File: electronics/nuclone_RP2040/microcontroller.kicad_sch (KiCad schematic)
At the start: 19 parts, among them Y1 12MHz

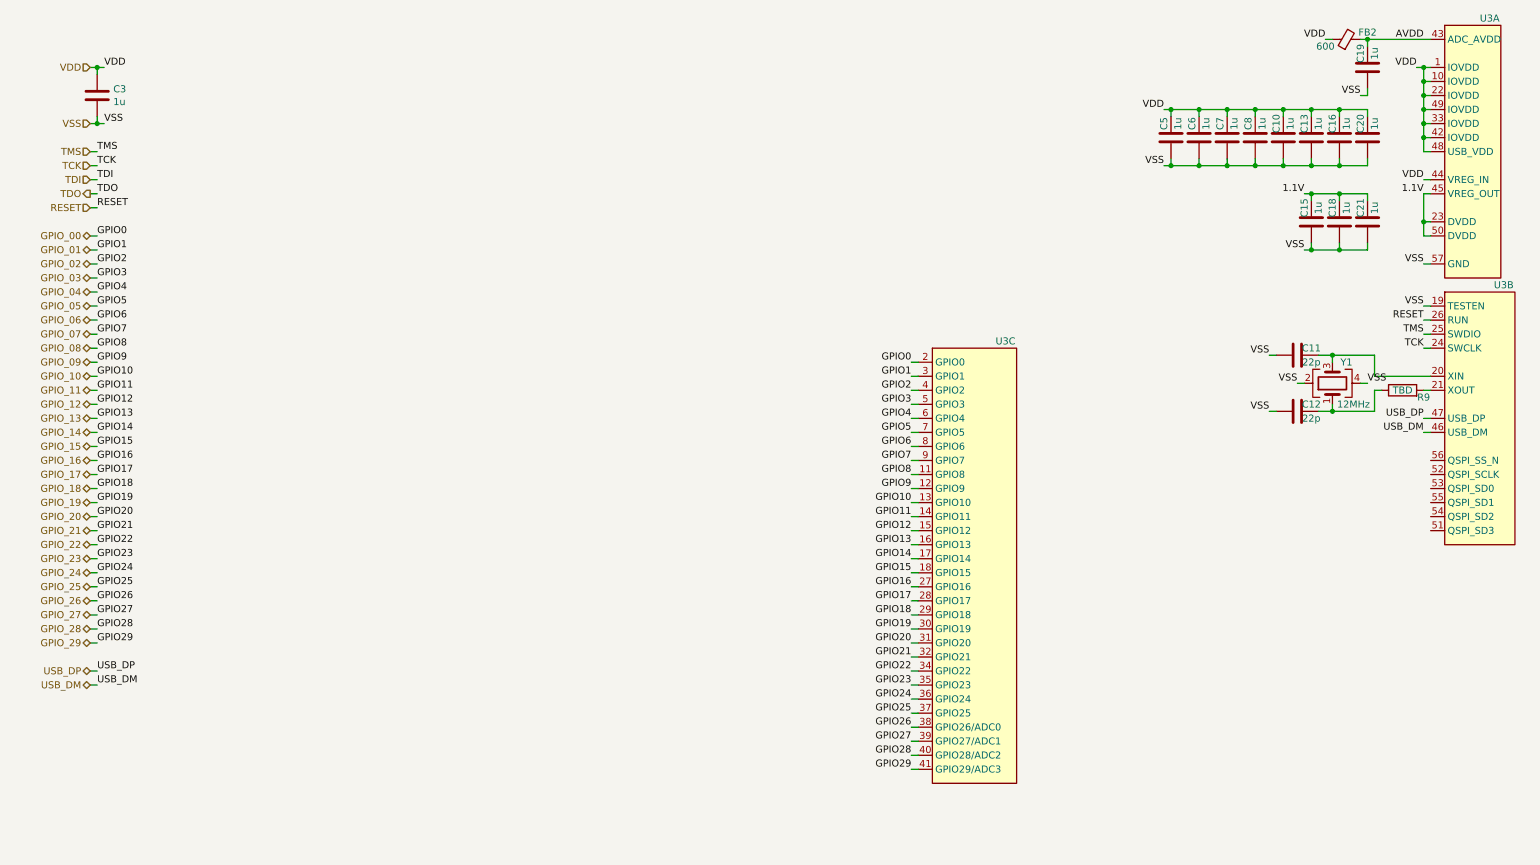
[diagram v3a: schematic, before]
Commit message: added QSPI flash
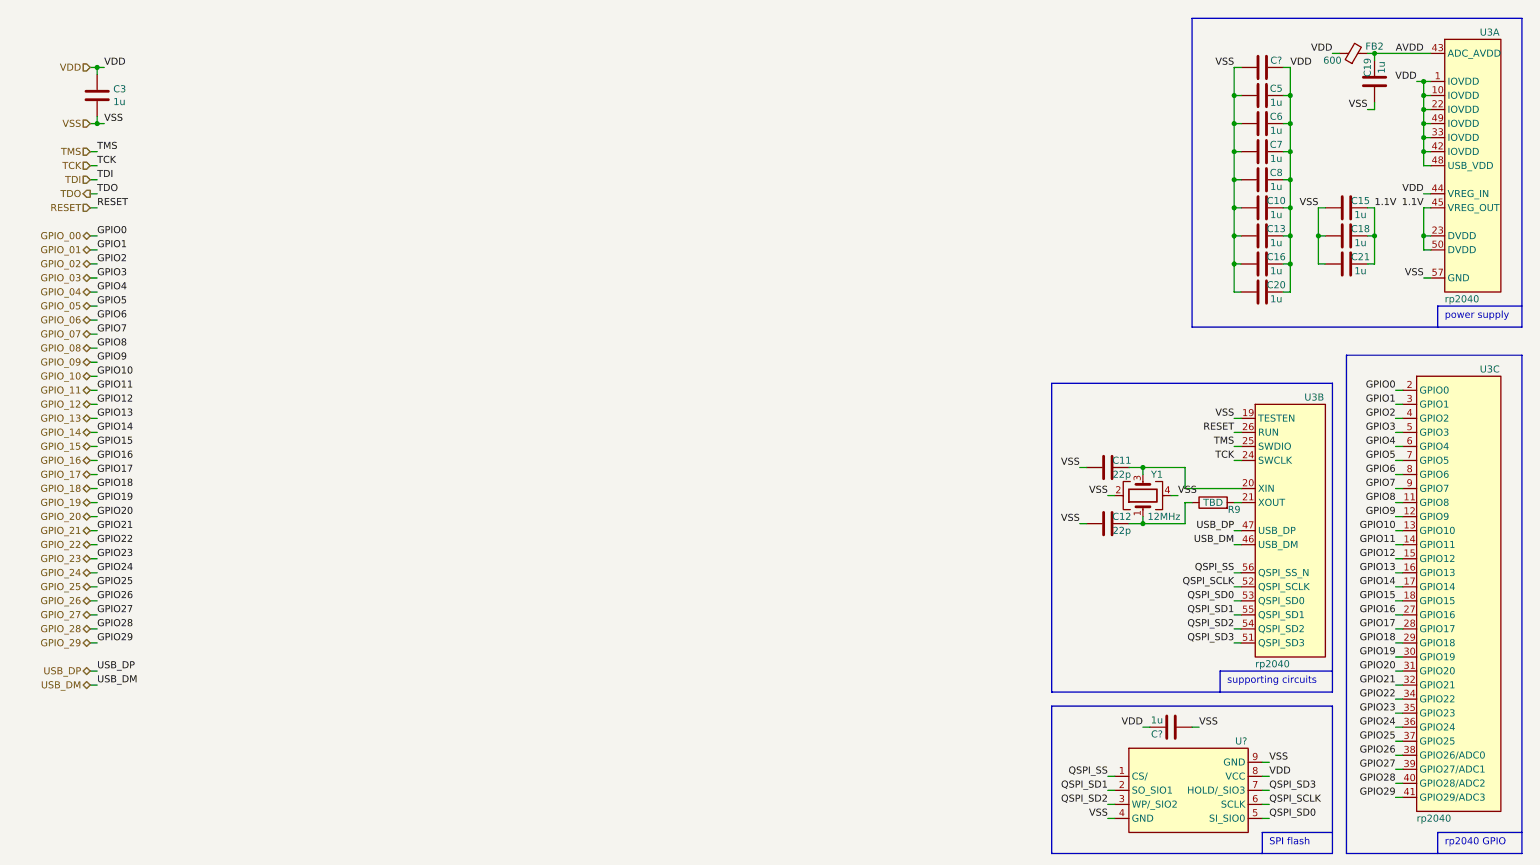
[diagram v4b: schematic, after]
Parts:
- added C?: 1u, SquantorRcl:C_0402, symbol Device:C
- added C?: (no value), symbol Device:C
- added U?: (no value), symbol SquantorGenericDigital:25X_9pin_QSPI_flash
- U3: value (none) -> rp2040; footprint (none) -> SquantorIC:QFN56_7by7mm_RaspberryPi
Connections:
- net VDD: now also C?.2, C?.2, U?.8 (VCC)
- net VSS: now also C?.1, C?.1, U?.4 (GND), U?.9 (GND)
- net QSPI_SD3: now reaches U3.51 (QSPI_SD3)
- net QSPI_SD3: now also U?.7 (HOLD/_SIO3)
- net QSPI_SCLK: now reaches U3.52 (QSPI_SCLK)
- net QSPI_SCLK: now also U?.6 (SCLK)
- net QSPI_SD0: now reaches U3.53 (QSPI_SD0)
- net QSPI_SD0: now also U?.5 (SI_SIO0)
- net QSPI_SD2: now reaches U3.54 (QSPI_SD2)
- net QSPI_SD2: now also U?.3 (WP/_SIO2)
- net QSPI_SD1: now reaches U3.55 (QSPI_SD1)
- net QSPI_SD1: now also U?.2 (SO_SIO1)
- net QSPI_SS: now reaches U3.56 (QSPI_SS_N)
- net QSPI_SS: now also U?.1 (CS/)
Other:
- note added: "SPI flash"
- note added: "power supply"
- note added: "rp2040 GPIO"
- note added: "supporting circuits"
- moved on the sheet: C10, C11, C12, C13, C15, C16, C18, C19, C20, C21, C5, C6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

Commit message: added serial flash
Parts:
- gave numbers to parts that had none: 3
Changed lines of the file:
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@@
   (symbol (lib_id "Device:C") (at 219.71 142.24 270) (unit 1)
     (in_bom yes) (on_board yes)
-    (property "Reference" "C?" (id 0) (at 217.17 143.51 90))
+    (property "Reference" "C22" (id 0) (at 217.17 143.51 90))
     (property "Value" "1u" (id 1) (at 217.17 140.97 90))
     (property "Footprint" "SquantorRcl:C_0402" (id 2) (at 215.9 143.2052 0)
@@
   (symbol (lib_id "SquantorGenericDigital:25X_9pin_QSPI_flash") (at 223.52 154.94 0) (unit 1)
     (in_bom yes) (on_board yes)
-    (property "Reference" "U?" (id 0) (at 232.41 144.78 0))
+    (property "Reference" "U4" (id 0) (at 232.41 144.78 0))
     (property "Value" "" (id 1) (at 219.71 162.56 0))
     (property "Footprint" "" (id 2) (at 223.52 154.94 0)
@@
   (symbol (lib_id "Device:C") (at 236.22 22.86 90) (unit 1)
     (in_bom yes) (on_board yes)
-    (property "Reference" "C?" (id 0) (at 238.76 21.59 90))
+    (property "Reference" "C23" (id 0) (at 238.76 21.59 90))
     (property "Value" "" (id 1) (at 238.76 24.13 90))
     (property "Footprint" "" (id 2) (at 240.03 21.8948 0)

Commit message: further placing and routing
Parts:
- added TP10: QSPI_SD2, SquantorTestPoints:TestPoint_hole_H04R07, symbol SquantorProto:testpad
- added TP11: QSPI_SD3, SquantorTestPoints:TestPoint_hole_H04R07, symbol SquantorProto:testpad
- added TP6: QSPI_SS, SquantorTestPoints:TestPoint_hole_H04R07, symbol SquantorProto:testpad
- added TP7: QSPI_SCLK, SquantorTestPoints:TestPoint_hole_H04R07, symbol SquantorProto:testpad
- added TP8: QSPI_SD0, SquantorTestPoints:TestPoint_hole_H04R07, symbol SquantorProto:testpad
- added TP9: QSPI_SD1, SquantorTestPoints:TestPoint_hole_H04R07, symbol SquantorProto:testpad
- C23: value (none) -> 10u; footprint (none) -> SquantorRcl:C_0603
- U4: value (none) -> MX25L3233FZBI; footprint (none) -> SquantorIC:USON-8-4x3-Macronix
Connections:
- net QSPI_SCLK: now also TP7.1
- net QSPI_SD0: now also TP8.1
- net QSPI_SD1: now also TP9.1
- net QSPI_SD2: now also TP10.1
- net QSPI_SD3: now also TP11.1
- net QSPI_SS: now also TP6.1
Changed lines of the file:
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@@
-    (stroke (width 0) (type default) (color 0 0 0 0))
-  )
-  (wire (pts (xy 231.14 121.92) (xy 232.41 121.92))
     (stroke (width 0) (type default) (color 0 0 0 0))
   )
@@
     (stroke (width 0) (type default) (color 0 0 0 0))
   )
-  (wire (pts (xy 231.14 119.38) (xy 232.41 119.38))
-    (stroke (width 0) (type default) (color 0 0 0 0))
-  )
   (wire (pts (xy 260.35 99.06) (xy 261.62 99.06))
     (stroke (width 0) (type default) (color 0 0 0 0))
@@
     (stroke (width 0) (type default) (color 0 0 0 0))
   )
-  (wire (pts (xy 231.14 114.3) (xy 232.41 114.3))
+  (wire (pts (xy 217.17 114.3) (xy 232.41 114.3))
     (stroke (width 0) (type default) (color 0 0 0 0))
   )
@@
     (stroke (width 0) (type default) (color 0 0 0 0))
   )
-  (wire (pts (xy 231.14 127) (xy 232.41 127))
+  (wire (pts (xy 217.17 127) (xy 232.41 127))
     (stroke (width 0) (type default) (color 0 0 0 0))
   )
@@
     (stroke (width 0) (type default) (color 0 0 0 0))
   )
-  (wire (pts (xy 231.14 116.84) (xy 232.41 116.84))
+  (wire (pts (xy 217.17 116.84) (xy 232.41 116.84))
     (stroke (width 0) (type default) (color 0 0 0 0))
   )
@@
     (stroke (width 0) (type default) (color 0 0 0 0))
   )
+  (wire (pts (xy 217.17 121.92) (xy 232.41 121.92))
+    (stroke (width 0) (type default) (color 0 0 0 0))
+  )
   (wire (pts (xy 260.35 116.84) (xy 261.62 116.84))
     (stroke (width 0) (type default) (color 0 0 0 0))
@@
     (stroke (width 0) (type default) (color 0 0 0 0))
   )
+  (wire (pts (xy 217.17 124.46) (xy 232.41 124.46))
+    (stroke (width 0) (type default) (color 0 0 0 0))
+  )
   (wire (pts (xy 203.2 95.25) (xy 204.47 95.25))
     (stroke (width 0) (type default) (color 0 0 0 0))
@@
     (stroke (width 0) (type default) (color 0 0 0 0))
   )
+  (wire (pts (xy 217.17 119.38) (xy 232.41 119.38))
+    (stroke (width 0) (type default) (color 0 0 0 0))
+  )
   (wire (pts (xy 241.3 27.94) (xy 240.03 27.94))
     (stroke (width 0) (type default) (color 0 0 0 0))
@@
   )
   (wire (pts (xy 241.3 58.42) (xy 241.3 63.5))
-    (stroke (width 0) (type default) (color 0 0 0 0))
-  )
-  (wire (pts (xy 231.14 124.46) (xy 232.41 124.46))
     (stroke (width 0) (type default) (color 0 0 0 0))
   )
@@
     (pin "2")
   )
+  (symbol (lib_id "SquantorProto:testpad") (at 214.63 127 180) (unit 1)
+    (in_bom yes) (on_board yes)
+    (property "Reference" "TP11" (id 0) (at 218.44 128.27 0))
+    (property "Value" "QSPI_SD3" (id 1) (at 208.28 127 0))
+    (property "Footprint" "SquantorTestPoints:TestPoint_hole_H04R07" (id 2) (at 213.36 127.635 0)
+      (effects (font (size 1.27 1.27)) hide)
+    )
+    (property "Datasheet" "" (id 3) (at 213.36 127.635 0)
+      (effects (font (size 1.27 1.27)) hide)
+    )
+    (pin "1")
+  )
+  (symbol (lib_id "SquantorProto:testpad") (at 214.63 119.38 180) (unit 1)
+    (in_bom yes) (on_board yes)
+    (property "Reference" "TP8" (id 0) (at 218.44 120.65 0))
+    (property "Value" "QSPI_SD0" (id 1) (at 208.28 119.38 0))
+    (property "Footprint" "SquantorTestPoints:TestPoint_hole_H04R07" (id 2) (at 213.36 120.015 0)
+      (effects (font (size 1.27 1.27)) hide)
+    )
+    (property "Datasheet" "" (id 3) (at 213.36 120.015 0)
+      (effects (font (size 1.27 1.27)) hide)
+    )
+    (pin "1")
+  )
   (symbol (lib_id "SquantorGenericDigital:25X_9pin_QSPI_flash") (at 223.52 154.94 0) (unit 1)
     (in_bom yes) (on_board yes)
     (property "Reference" "U4" (id 0) (at 232.41 144.78 0))
-    (property "Value" "" (id 1) (at 219.71 162.56 0))
-    (property "Footprint" "" (id 2) (at 223.52 154.94 0)
+    (property "Value" "MX25L3233FZBI" (id 1) (at 219.71 162.56 0))
+    (property "Footprint" "SquantorIC:USON-8-4x3-Macronix" (id 2) (at 223.52 154.94 0)
       (effects (font (size 1.27 1.27)) hide)
     )
@@
     (pin "9")
   )
+  (symbol (lib_id "SquantorProto:testpad") (at 214.63 114.3 180) (unit 1)
+    (in_bom yes) (on_board yes)
+    (property "Reference" "TP6" (id 0) (at 218.44 115.57 0))
+    (property "Value" "QSPI_SS" (id 1) (at 208.28 114.3 0))
+    (property "Footprint" "SquantorTestPoints:TestPoint_hole_H04R07" (id 2) (at 213.36 114.935 0)
+      (effects (font (size 1.27 1.27)) hide)
+    )
+    (property "Datasheet" "" (id 3) (at 213.36 114.935 0)
+      (effects (font (size 1.27 1.27)) hide)
+    )
+    (pin "1")
+  )
   (symbol (lib_id "Device:C") (at 251.46 53.34 90) (unit 1)
     (in_bom yes) (on_board yes)
@@
     (pin "2")
   )
+  (symbol (lib_id "SquantorProto:testpad") (at 214.63 124.46 180) (unit 1)
+    (in_bom yes) (on_board yes)
+    (property "Reference" "TP10" (id 0) (at 218.44 125.73 0))
+    (property "Value" "QSPI_SD2" (id 1) (at 208.28 124.46 0))
+    (property "Footprint" "SquantorTestPoints:TestPoint_hole_H04R07" (id 2) (at 213.36 125.095 0)
+      (effects (font (size 1.27 1.27)) hide)
+    )
+    (property "Datasheet" "" (id 3) (at 213.36 125.095 0)
+      (effects (font (size 1.27 1.27)) hide)
+    )
+    (pin "1")
+  )
   (symbol (lib_id "Device:C") (at 236.22 58.42 90) (unit 1)
     (in_bom yes) (on_board yes)
@@
     (pin "2")
   )
+  (symbol (lib_id "SquantorProto:testpad") (at 214.63 116.84 180) (unit 1)
+    (in_bom yes) (on_board yes)
+    (property "Reference" "TP7" (id 0) (at 218.44 118.11 0))
+    (property "Value" "QSPI_SCLK" (id 1) (at 208.28 116.84 0))
+    (property "Footprint" "SquantorTestPoints:TestPoint_hole_H04R07" (id 2) (at 213.36 117.475 0)
+      (effects (font (size 1.27 1.27)) hide)
+    )
+    (property "Datasheet" "" (id 3) (at 213.36 117.475 0)
+      (effects (font (size 1.27 1.27)) hide)
+    )
+    (pin "1")
+  )
   (symbol (lib_id "Device:Crystal_GND24") (at 214.63 100.33 90) (unit 1)
     (in_bom yes) (on_board yes)
@@
     (in_bom yes) (on_board yes)
     (property "Reference" "C23" (id 0) (at 238.76 21.59 90))
-    (property "Value" "" (id 1) (at 238.76 24.13 90))
-    (property "Footprint" "" (id 2) (at 240.03 21.8948 0)
+    (property "Value" "10u" (id 1) (at 238.76 24.13 90))
+    (property "Footprint" "SquantorRcl:C_0603" (id 2) (at 240.03 21.8948 0)
       (effects (font (size 1.27 1.27)) hide)
     )
@@
     (pin "2")
   )
+  (symbol (lib_id "SquantorProto:testpad") (at 214.63 121.92 180) (unit 1)
+    (in_bom yes) (on_board yes)
+    (property "Reference" "TP9" (id 0) (at 218.44 123.19 0))
+    (property "Value" "QSPI_SD1" (id 1) (at 208.28 121.92 0))
+    (property "Footprint" "SquantorTestPoints:TestPoint_hole_H04R07" (id 2) (at 213.36 122.555 0)
+      (effects (font (size 1.27 1.27)) hide)
+    )
+    (property "Datasheet" "" (id 3) (at 213.36 122.555 0)
+      (effects (font (size 1.27 1.27)) hide)
+    )
+    (pin "1")
+  )
   (symbol (lib_id "Device:C") (at 236.22 48.26 90) (unit 1)

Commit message: further routing, added a QSPI debug connector for easy probing with logic analyser
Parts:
- removed TP10: QSPI_SD2, SquantorTestPoints:TestPoint_hole_H04R07, symbol SquantorProto:testpad
- removed TP11: QSPI_SD3, SquantorTestPoints:TestPoint_hole_H04R07, symbol SquantorProto:testpad
- removed TP6: QSPI_SS, SquantorTestPoints:TestPoint_hole_H04R07, symbol SquantorProto:testpad
- removed TP7: QSPI_SCLK, SquantorTestPoints:TestPoint_hole_H04R07, symbol SquantorProto:testpad
- removed TP8: QSPI_SD0, SquantorTestPoints:TestPoint_hole_H04R07, symbol SquantorProto:testpad
- removed TP9: QSPI_SD1, SquantorTestPoints:TestPoint_hole_H04R07, symbol SquantorProto:testpad
- added J5: Conn_02x06_Odd_Even, SquantorConnectors:Header-0127-2X06-H006, symbol Connector_Generic:Conn_02x06_Odd_Even
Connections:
- net QSPI_SCLK: now also J5.4 (Pin_4)
- net QSPI_SD0: now also J5.6 (Pin_6)
- net QSPI_SD1: now also J5.10 (Pin_10)
- net QSPI_SD2: now also J5.8 (Pin_8)
- net QSPI_SD3: now also J5.2 (Pin_2)
- net QSPI_SS: now also J5.12 (Pin_12)
- net VSS: now also J5.1 (Pin_1), J5.11 (Pin_11), J5.3 (Pin_3), J5.5 (Pin_5), J5.7 (Pin_7), J5.9 (Pin_9)
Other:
- note added: "QSPI debug connector"

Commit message: more alignment to official schematic
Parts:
- added R10: DNF, SquantorRcl:R_0402_hand, symbol Device:R
- added R11: 1K, SquantorRcl:R_0402_hand, symbol Device:R
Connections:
- net QSPI_SS: now also R10.2, R11.2
- net VDD: now also R10.1
- new net bootloader: R11.1
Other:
- moved on the sheet: C11, C12, C22, J5, R9, U3B, U3C, U4, Y1
